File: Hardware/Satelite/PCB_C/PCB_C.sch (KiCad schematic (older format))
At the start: 46 parts, among them IC1 MCP1501T-33E_CHY, J3 Conector_PCB_B-C, J4 Conector_Expansion_CanSat, J5 USB_B_Micro, M1 Spacer, M2 Spacer, M3 Spacer, U1 TXS0104ERGYR, U2 TCA9802DGKR, U3 W25Q32JVSSIQ, U4 TXS0104ERGYR, U5 BL654, Y1 LFXTAL016178

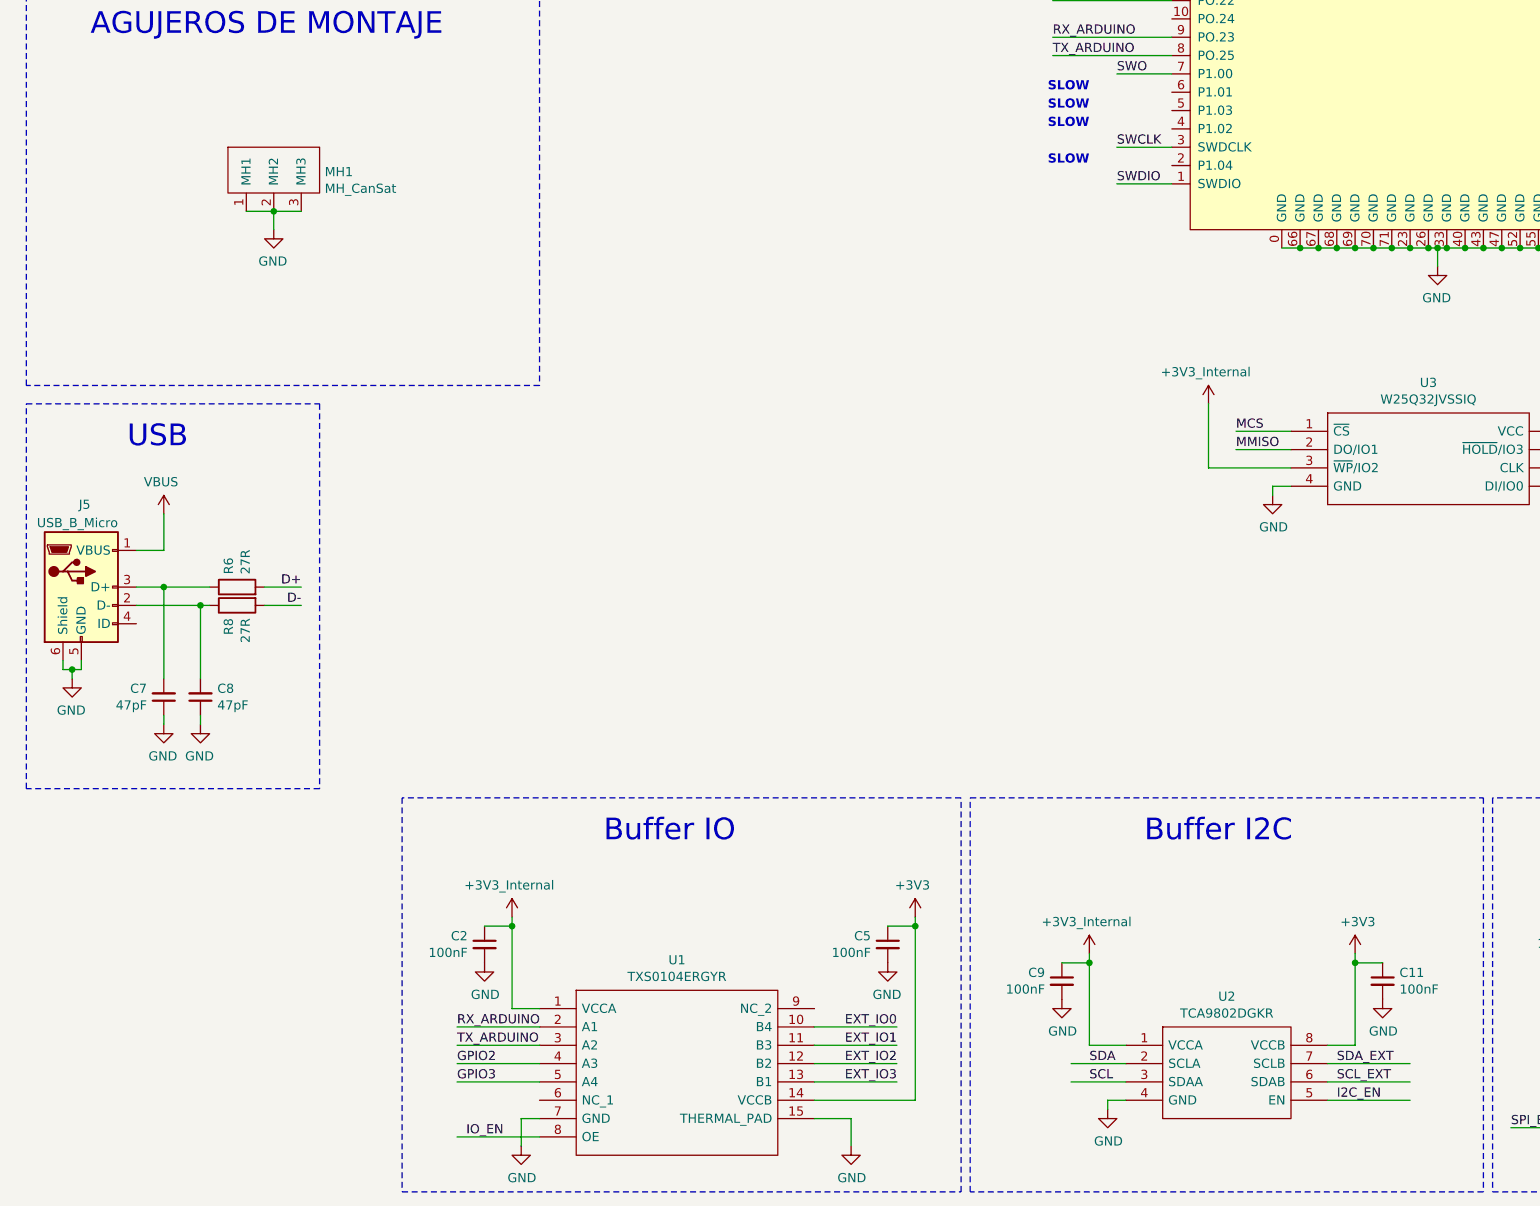
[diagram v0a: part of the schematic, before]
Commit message: Agregado conector de programación para el nRF52840
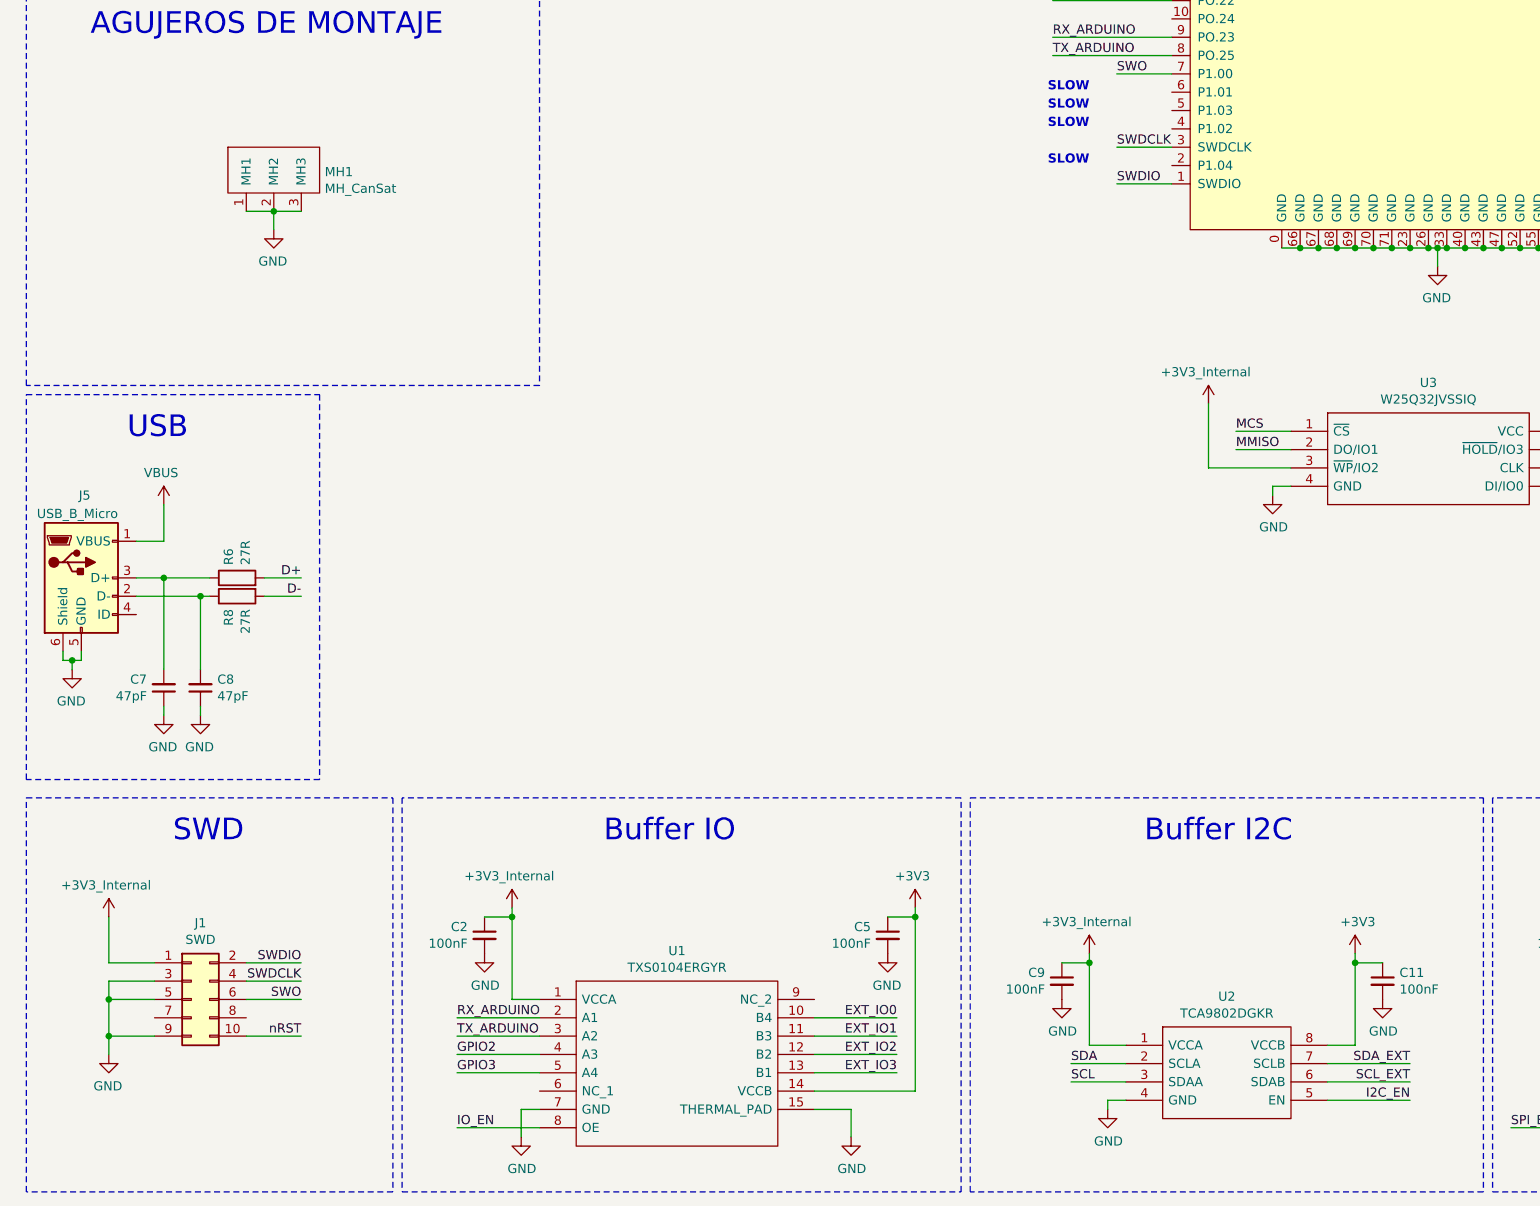
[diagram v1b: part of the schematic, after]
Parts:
- added J1: SWD, Connector_PinHeader_1.27mm:PinHeader_2x05_P1.27mm_Vertical_SMD, symbol Connector_Generic:Conn_02x05_Odd_Even
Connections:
- net labels added: SWDCLK
- net labels removed: SWCLK
- wire segments 297 -> 309
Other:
- note added: "SWD"
- moved on the sheet: C2, C5, C7, C8, J5, R6, R8, U1

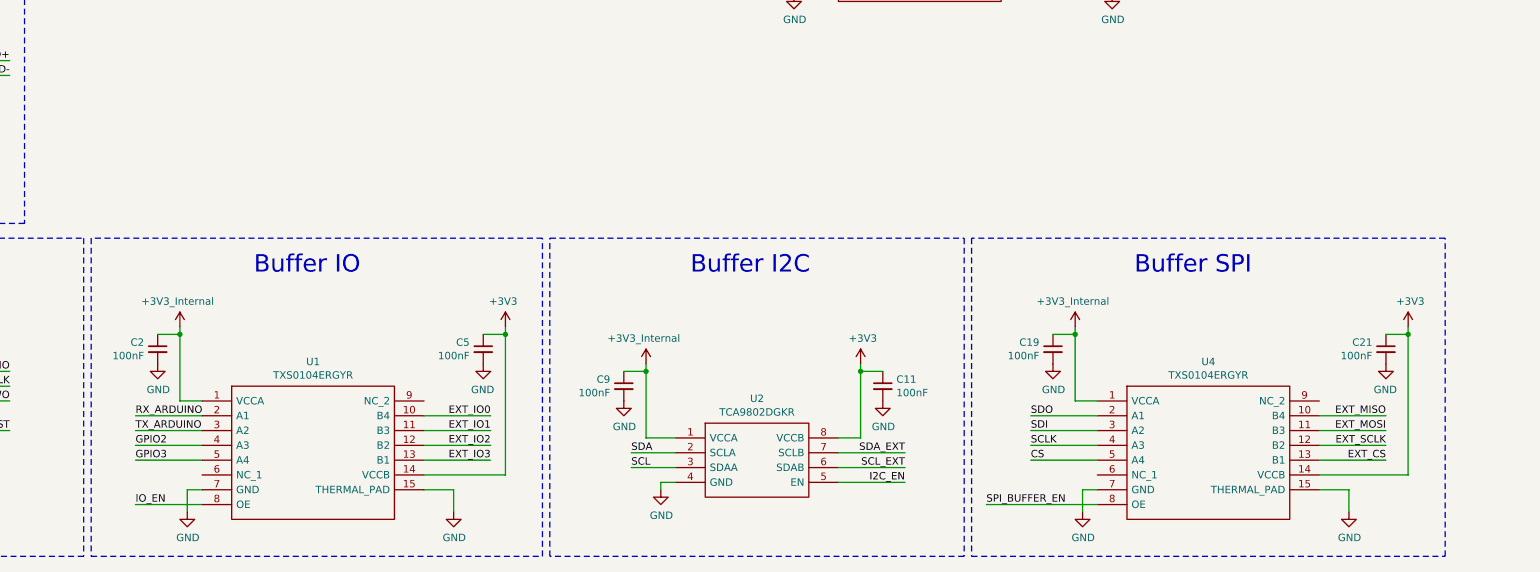
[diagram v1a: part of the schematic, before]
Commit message: Agregados R pull-down en buffers del PCB_C
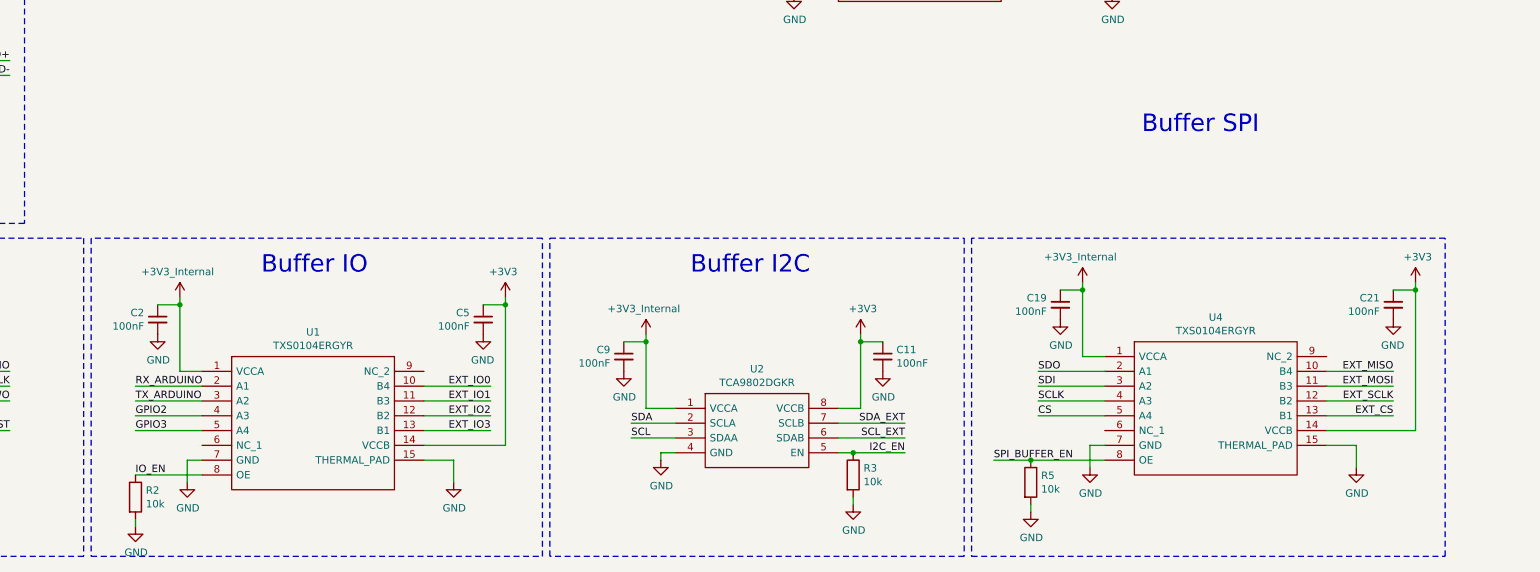
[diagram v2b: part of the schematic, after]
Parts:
- added R2, R3, R5: 10k, Resistor_SMD:R_0603_1608Metric_Pad1.05x0.95mm_HandSolder, symbol Device:R
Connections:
- wire segments 309 -> 314
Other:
- moved on the sheet: C11, C19, C2, C21, C5, C9, U1, U2, U4

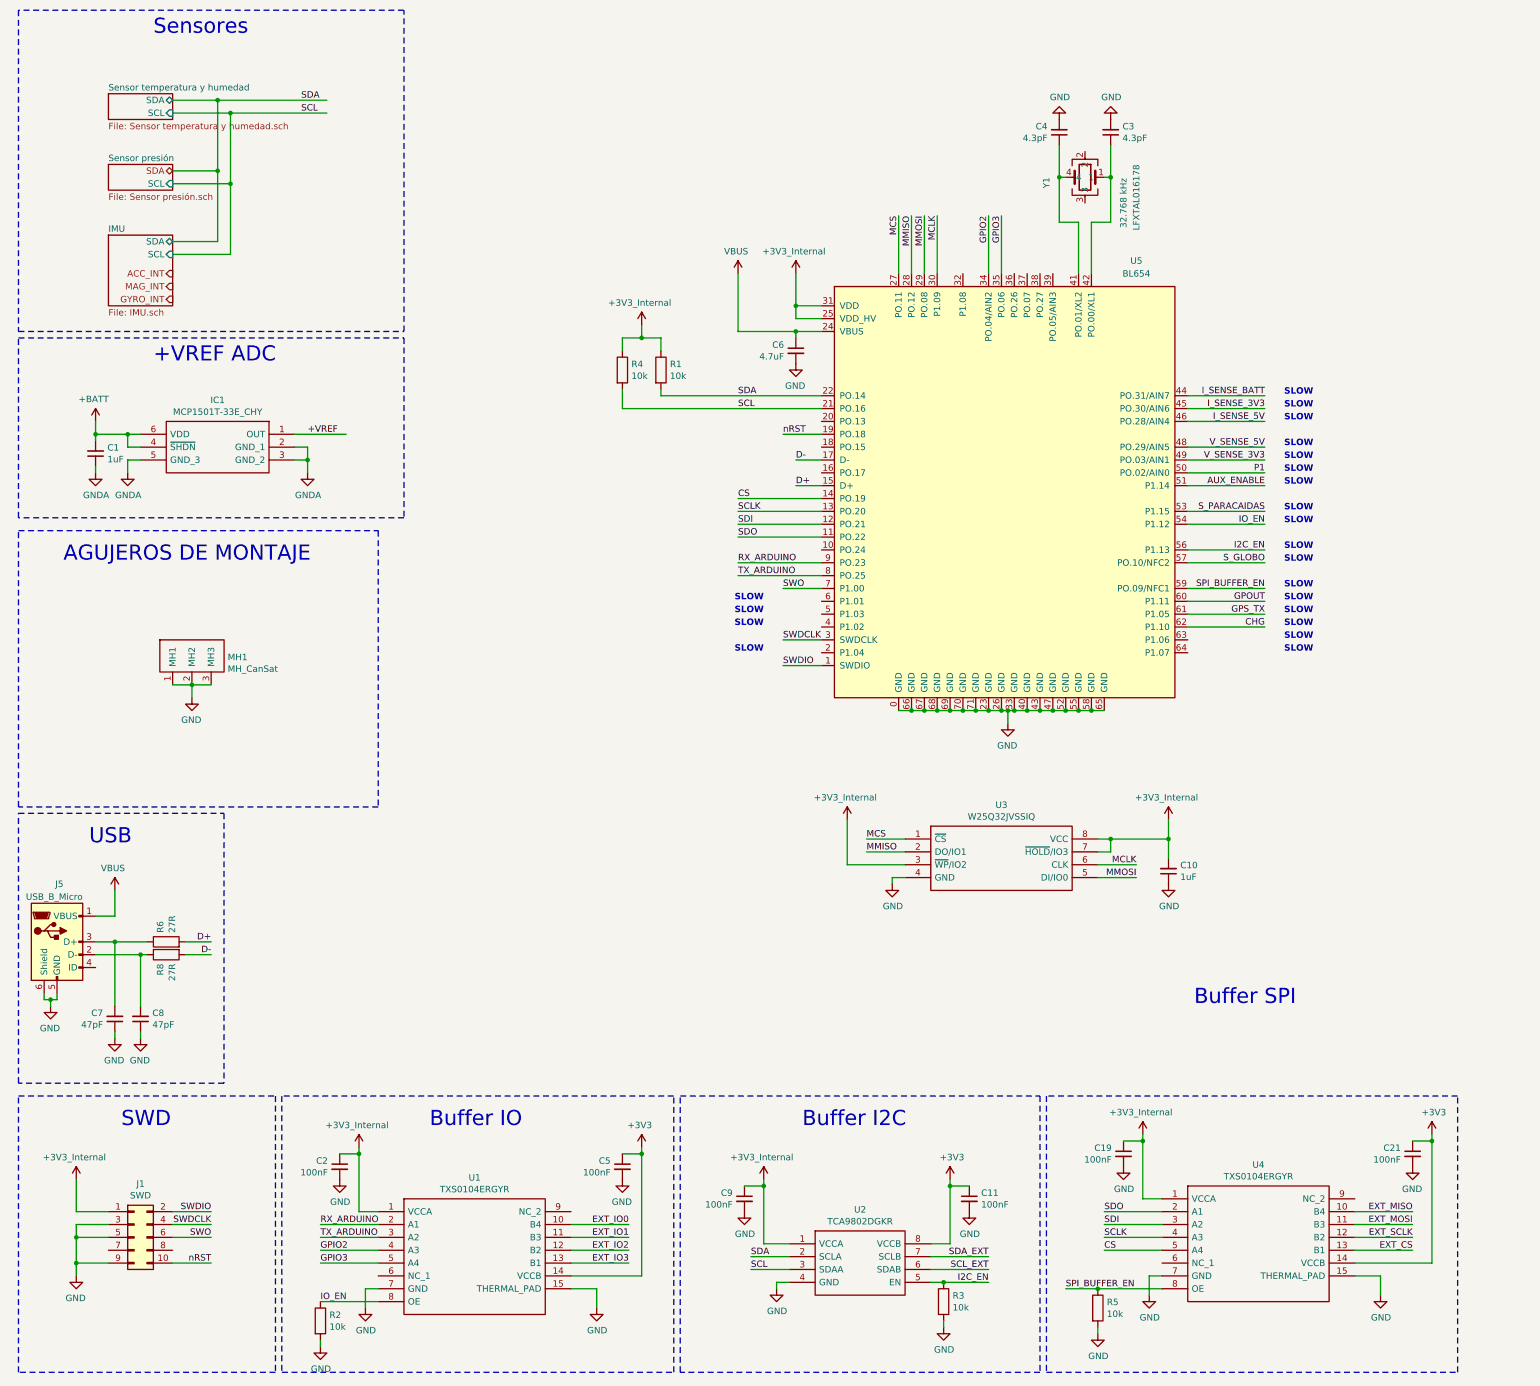
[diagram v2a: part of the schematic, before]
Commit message: Agregado sensor de temperatura de mayor precisión
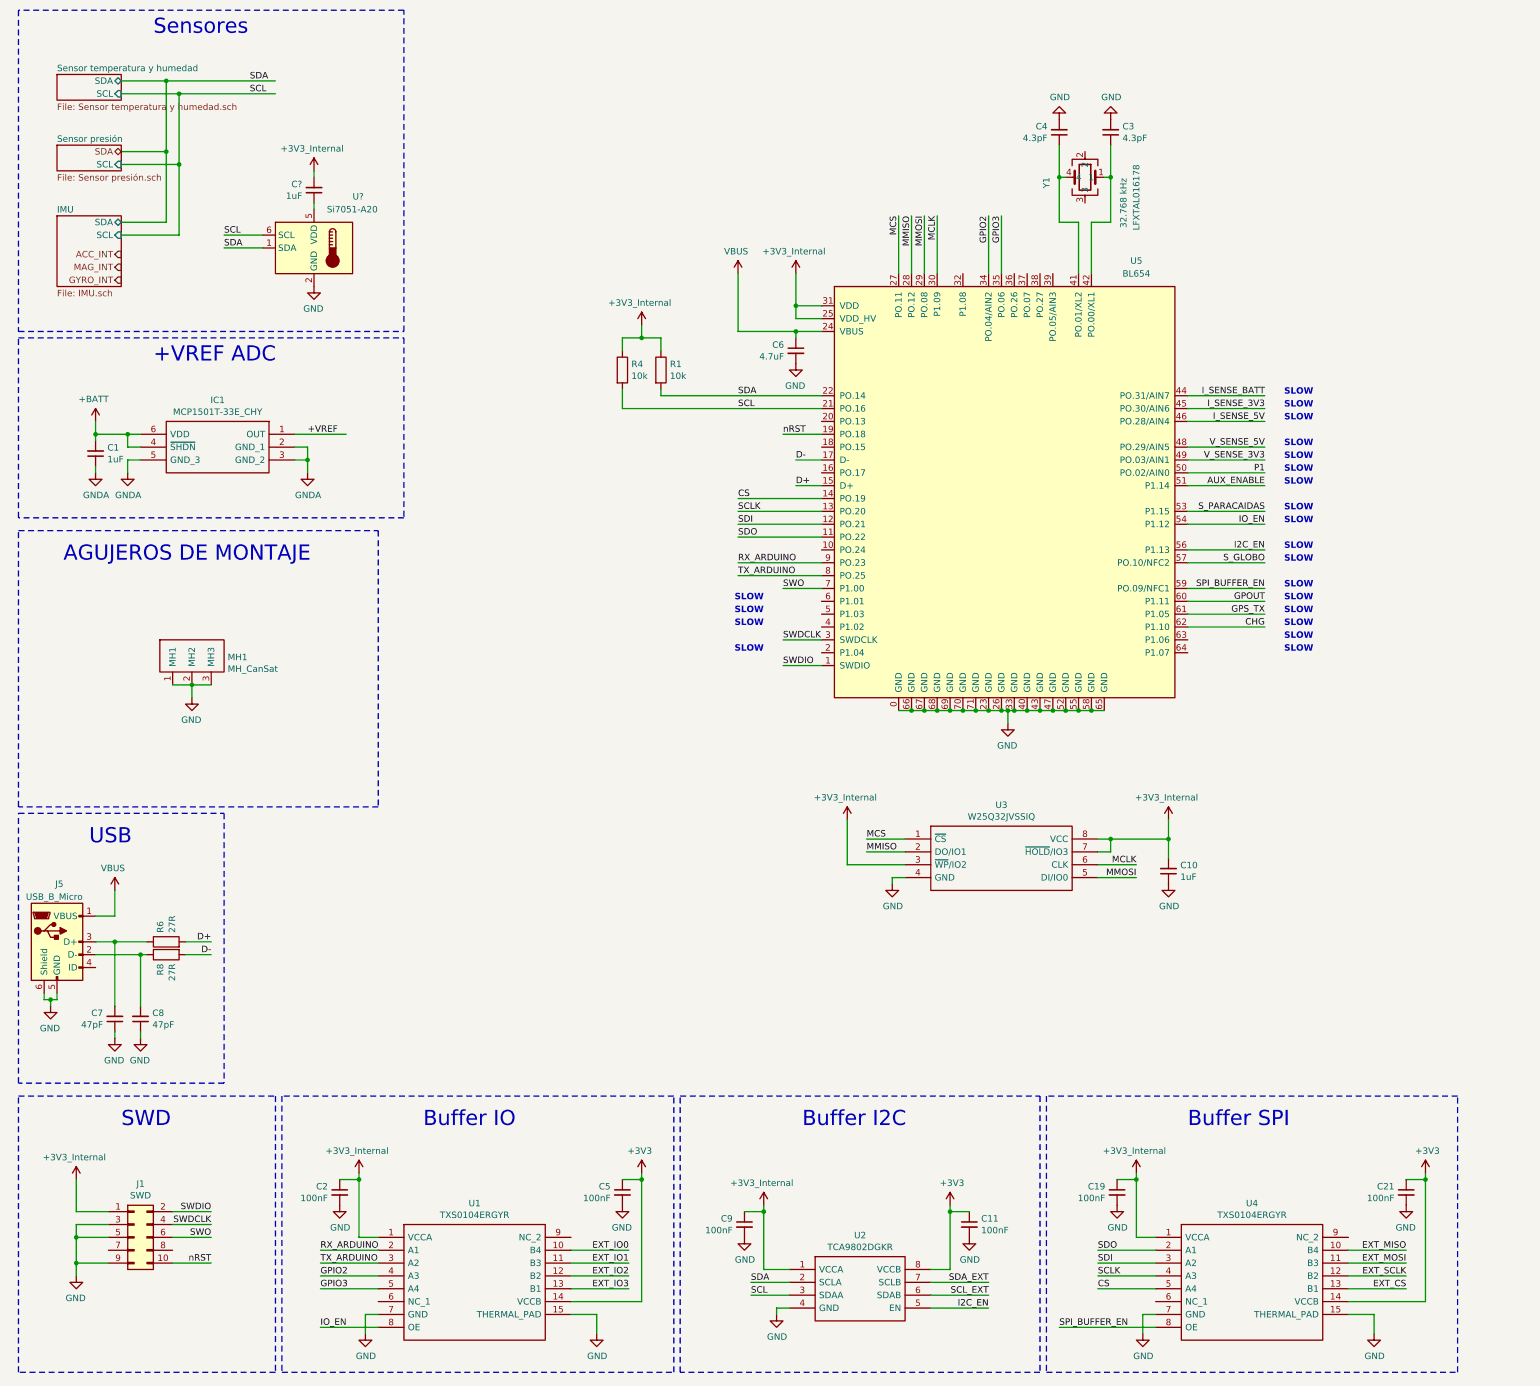
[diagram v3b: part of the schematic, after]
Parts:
- removed R2, R3, R5: 10k, Resistor_SMD:R_0603_1608Metric_Pad1.05x0.95mm_HandSolder, symbol Device:R
- added C?: 1uF, Capacitor_SMD:C_0402_1005Metric, symbol Device:C_Small
- added U?: Si7051-A20, Package_DFN_QFN:DFN-6-1EP_3x3mm_P1mm_EP1.65x2.55mm, symbol Sensor_Temperature:Si7051-A20
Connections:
- wire segments 314 -> 313
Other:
- moved on the sheet: C11, C19, C2, C21, C5, C9, U1, U2, U4
